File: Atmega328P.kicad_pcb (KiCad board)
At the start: 2 copper layers, 20 parts, among them J1 AVR-ISP-6, J2 FTDI, SW1 Reset, U1 LM1117-5.0, U2 ATmega328P-AU, Y1 Crystal

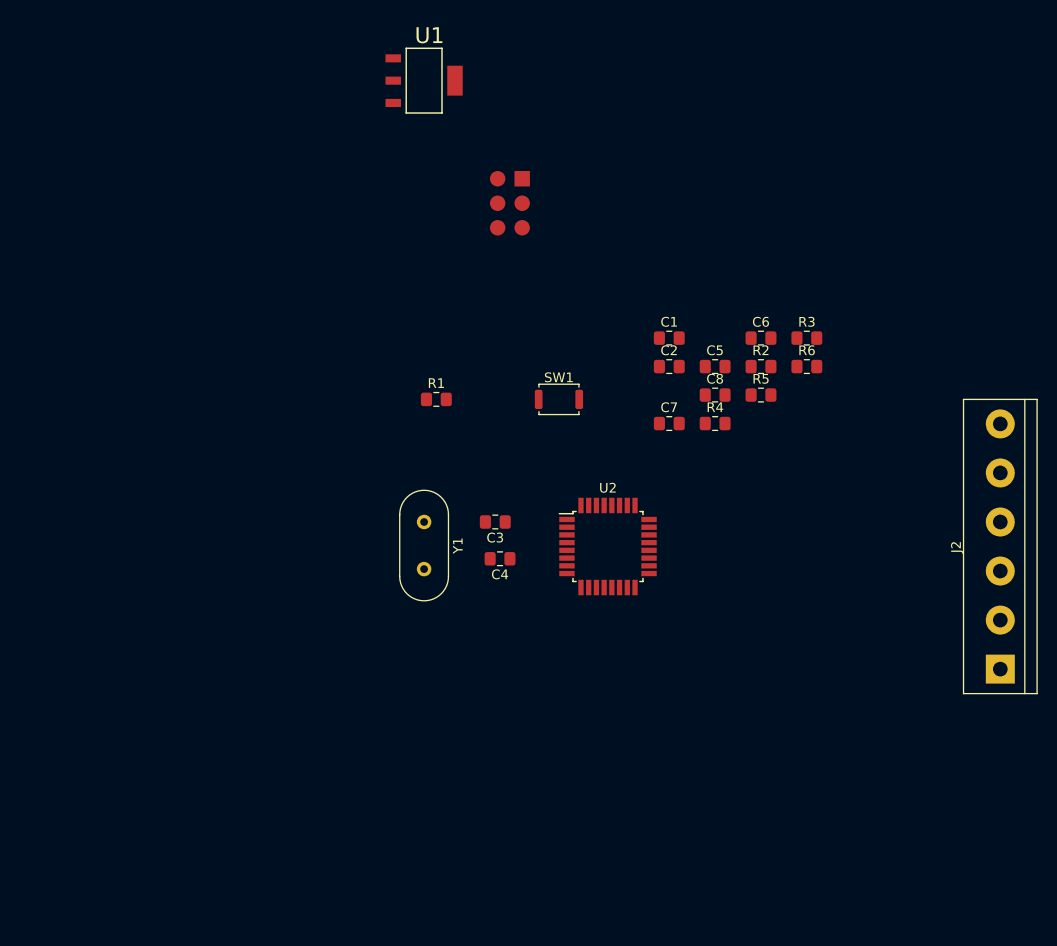
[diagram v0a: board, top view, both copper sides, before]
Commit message: Adds an alternative board layout and new footprints.
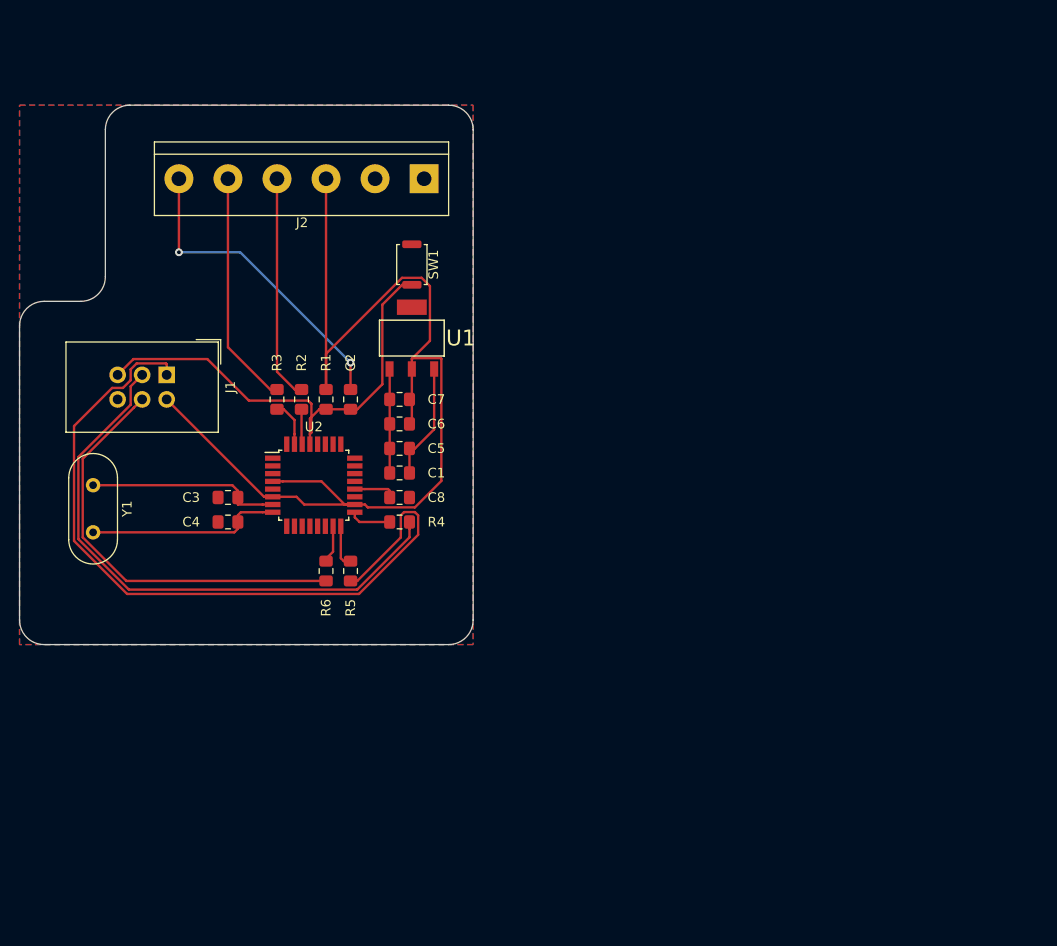
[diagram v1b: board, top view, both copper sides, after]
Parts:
- J1: footprint custom:AVR-ISP-6 -> custom:IDC-Header_2x03_Pitch2.54mm_Straight
- moved J2 78.4 mm to (128.3, 54.6), turned to 180 degrees
- moved R3 55.3 mm to (113.0, 77.5), turned to 270 degrees
- moved R6 54.1 mm to (118.1, 95.2), turned to 90 degrees
- moved R2 47.7 mm to (115.6, 77.5), turned to 270 degrees
- moved R5 46.3 mm to (120.7, 95.2), turned to 90 degrees
- moved J1 39.9 mm to (101.6, 74.9), turned to 270 degrees
- moved C6 38.5 mm to (125.7, 80.0), turned to 180 degrees
- moved Y1 34.5 mm to (94.0, 86.4)
- moved C8 34.4 mm to (125.7, 87.6)
- moved R4 34.2 mm to (125.7, 90.2), turned to 180 degrees
- moved C5 33.8 mm to (125.7, 82.5), turned to 180 degrees
- moved C2 33.2 mm to (120.7, 77.5), turned to 270 degrees
- moved C1 31.2 mm to (125.7, 85.1), turned to 180 degrees
- moved U2 31.1 mm to (116.8, 86.4)
- moved C4 28.4 mm to (108.0, 90.2), turned to 0 degrees
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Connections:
- J1 pad 1: /D12 -> /MISO
- J1 pad 3: /D13 -> /SCK
- J1 pad 4: /D11 -> /MOSI
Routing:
- net +5V: track 0.00 -> 114.6 mm
- net /MISO: track 0.00 -> 79.9 mm
- net /SCK: track 0.00 -> 60.0 mm
- net /RESET: track 0.00 -> 49.6 mm
- net /MOSI: track 0.00 -> 43.9 mm
- net Net-(C2-Pad1): track 0.00 -> 32.9 mm, vias 0 -> 2
- net /TX: track 0.00 -> 24.3 mm
- net /RX: track 0.00 -> 23.3 mm
- net /XTAL2: track 0.00 -> 20.3 mm
- net /XTAL1: track 0.00 -> 20.3 mm
- net VCC: track 0.00 -> 12.2 mm
- net Net-(C1-Pad2): track 0.00 -> 10.8 mm
- net /D1: track 0.00 -> 4.77 mm
- net /D12: track 0.00 -> 4.44 mm
- net Net-(C8-Pad1): track 0.00 -> 4.39 mm
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- added copper zone on B.Cu, net Earth
- added copper zone on F.Cu, net Earth
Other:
- board outline added: 47 x 55.9 mm

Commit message: Modifies board layout
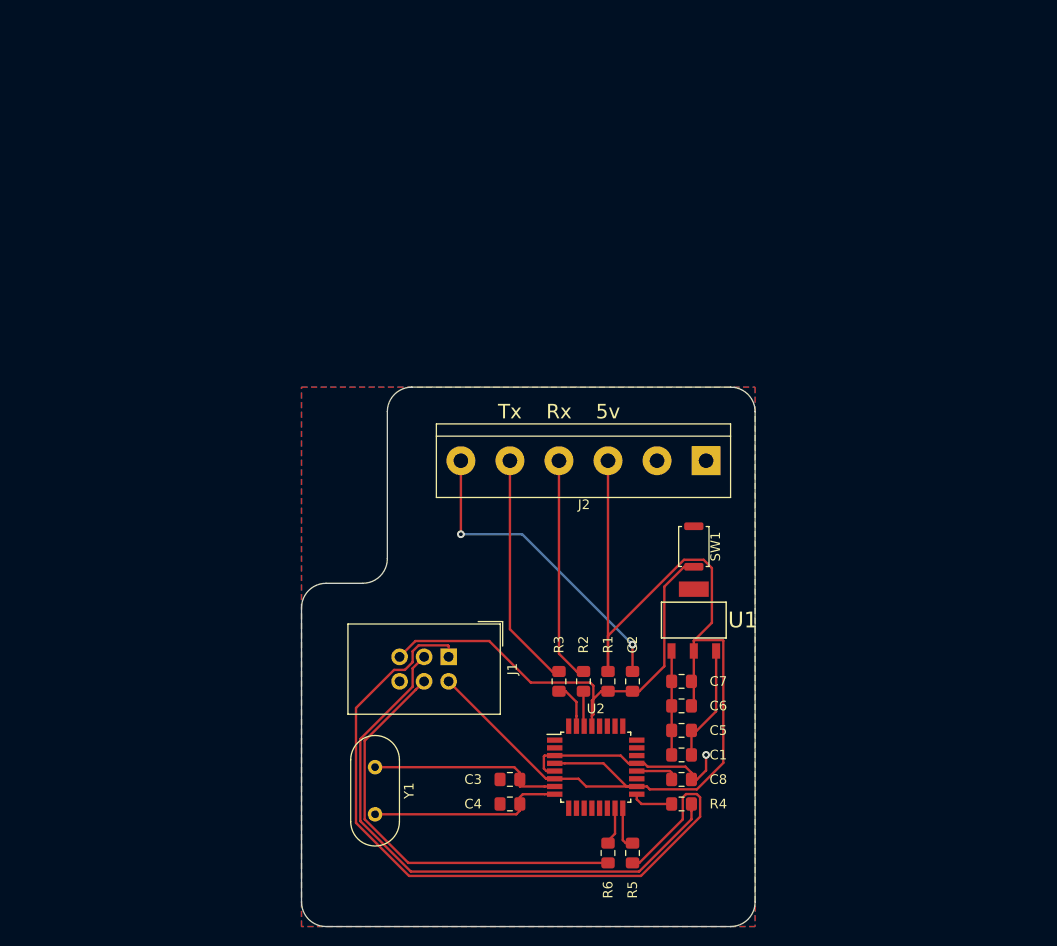
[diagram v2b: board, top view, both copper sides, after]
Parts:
- moved C2 41.3 mm to (149.9, 106.7)
- moved R2 41.3 mm to (144.8, 106.7)
- moved R3 41.3 mm to (142.2, 106.7)
- moved C3 41.3 mm to (137.2, 116.8)
- moved C5 41.3 mm to (154.9, 111.8)
- moved C7 41.3 mm to (154.9, 106.7)
- moved C8 41.3 mm to (154.9, 116.8)
- moved J1 41.3 mm to (130.8, 104.1)
- moved R1 41.3 mm to (147.3, 106.7)
- moved R5 41.3 mm to (149.9, 124.5)
- moved SW1 41.3 mm to (156.2, 92.7)
- moved U1 41.3 mm to (156.2, 100.3)
- moved U2 41.3 mm to (146.1, 115.6)
- moved C1 41.3 mm to (154.9, 114.3)
- moved C4 41.3 mm to (137.2, 119.4)
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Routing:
- net Earth: track 0.00 -> 22.8 mm, vias 0 -> 1
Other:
- outline, holes or cut-outs redrawn
- board text added: "5v"
- board text added: "Rx"
- board text added: "Tx"
